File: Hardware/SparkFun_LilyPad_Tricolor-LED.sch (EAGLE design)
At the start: 11 parts

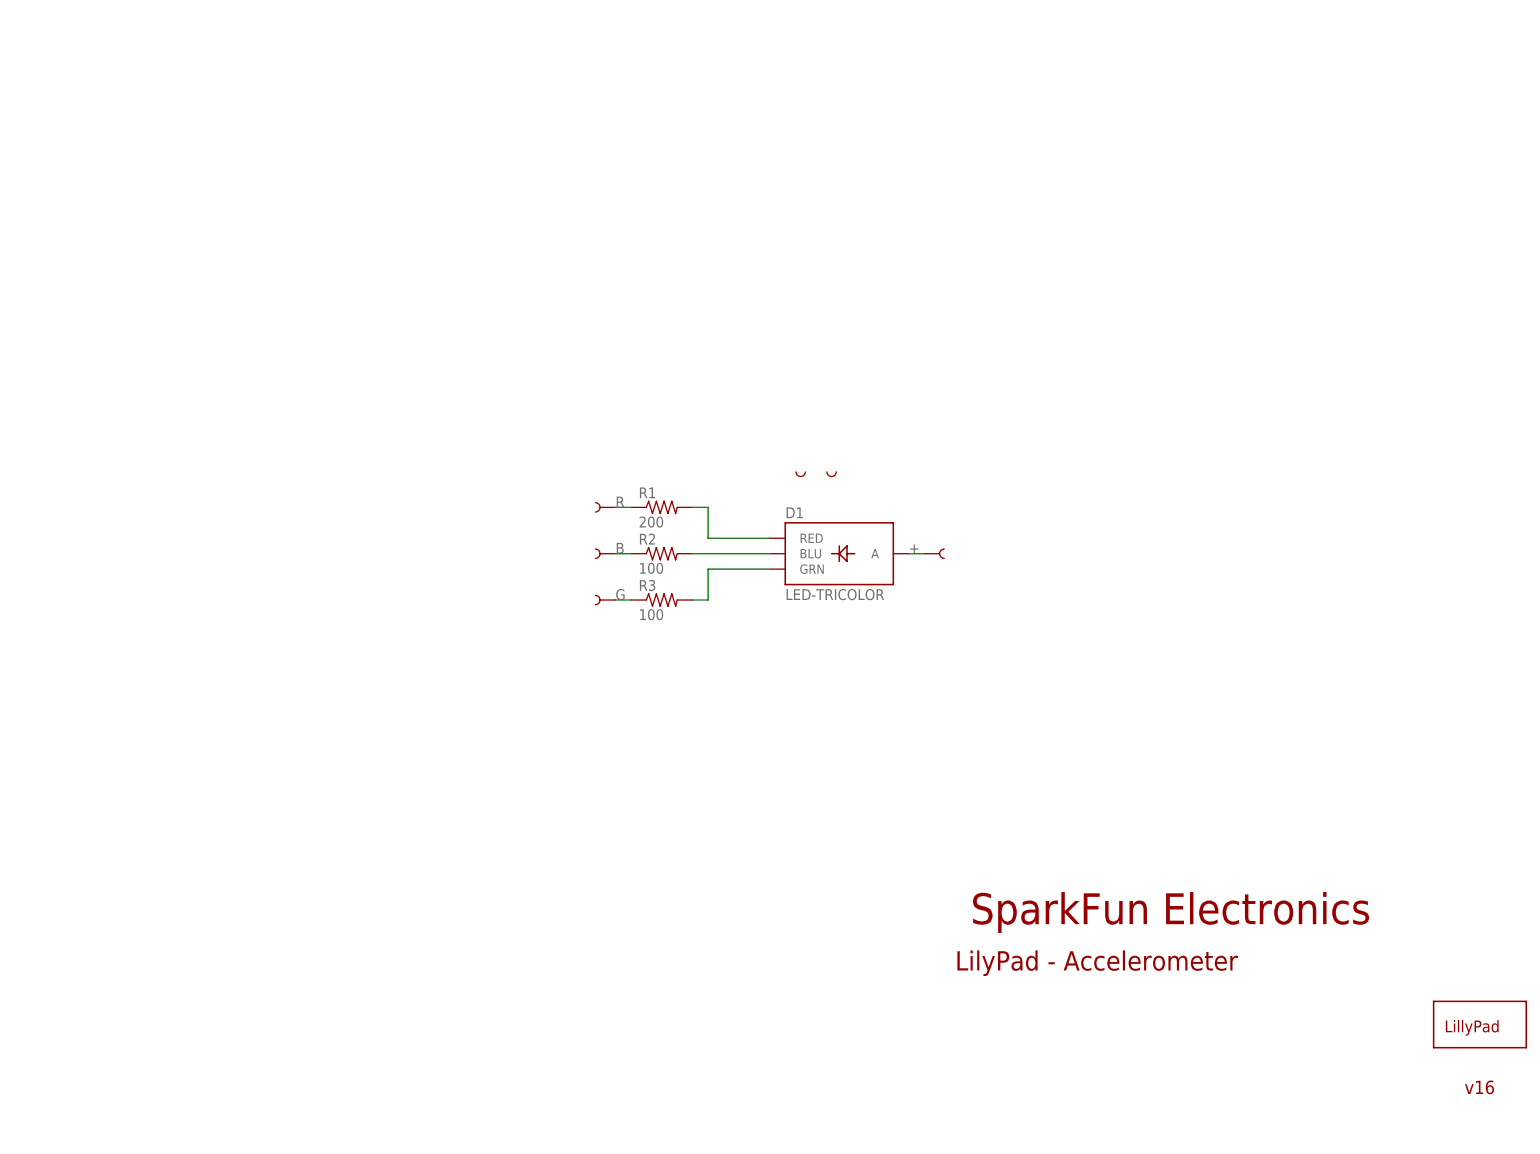
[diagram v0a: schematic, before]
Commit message: revising to common cathode LED
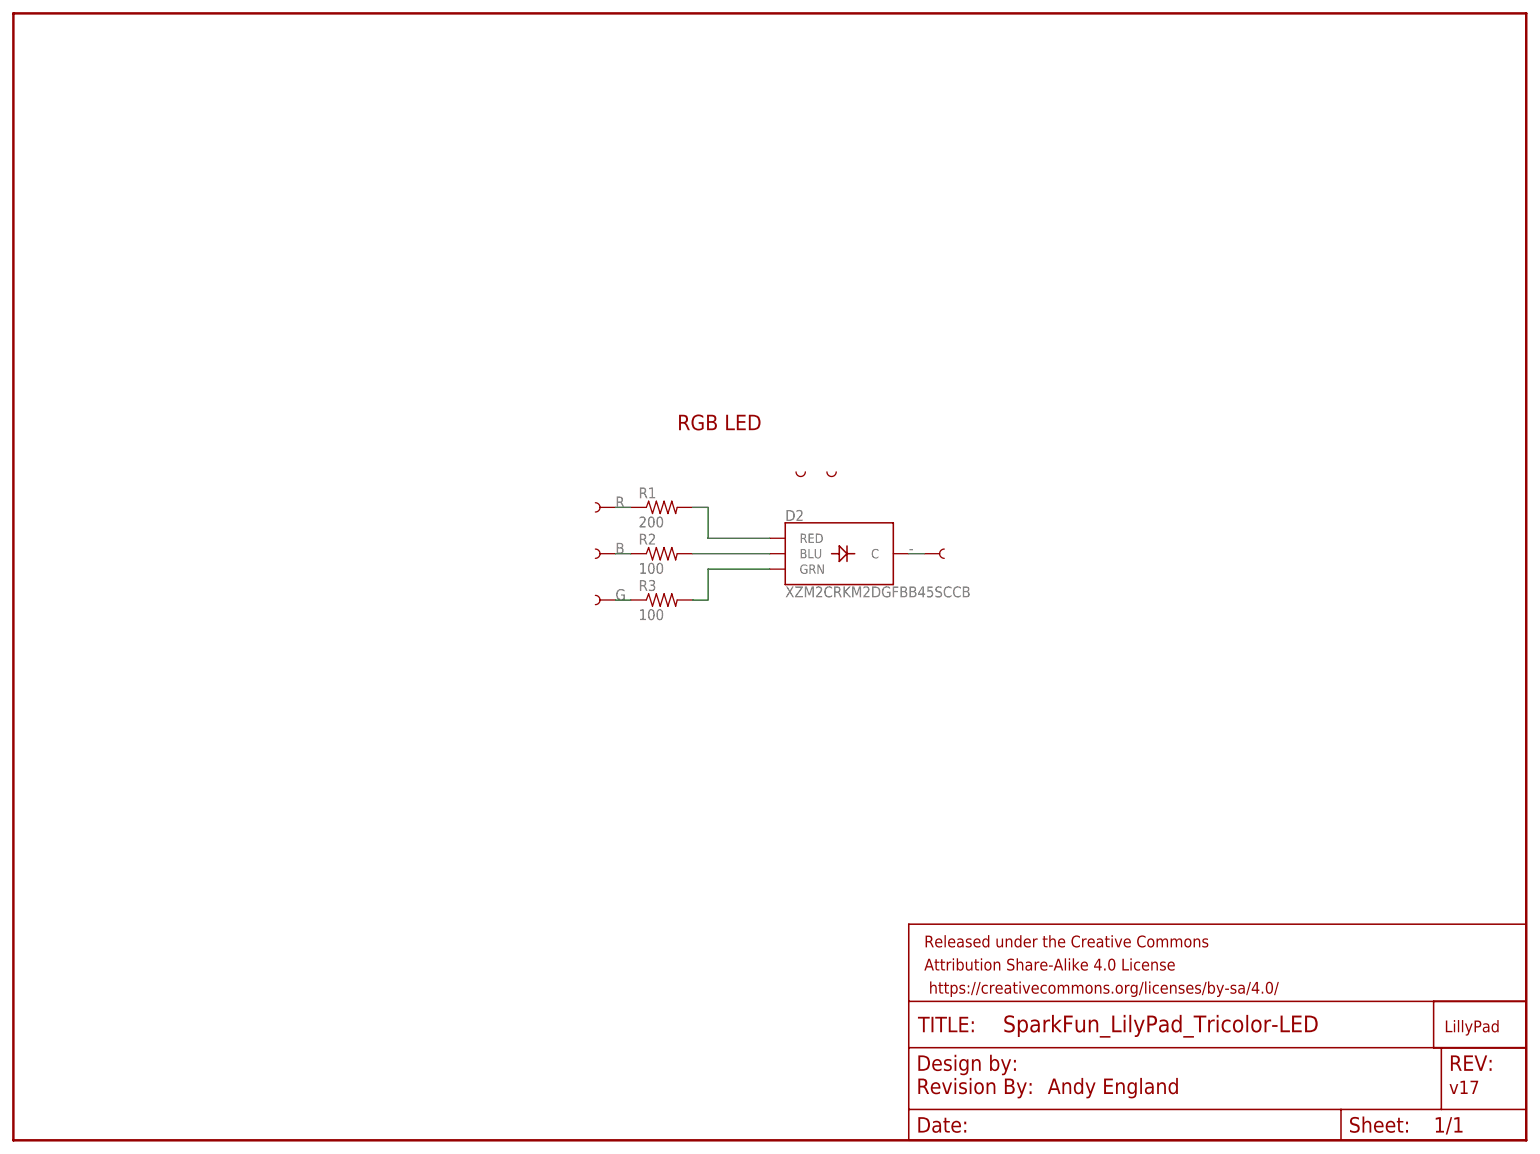
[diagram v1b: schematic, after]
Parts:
- removed D1: LED-TRICOLOR, SparkFun:LED-TRICOLOR
- added D2: XZM2CRKM2DGFBB45SCCB, SparkFun-LED:SUNLEDSMD1
- added FRAME1: FRAME-LETTER, SparkFun-Aesthetics:FRAME-LETTER
- added LOGO1: REVISION, SparkFun-Aesthetics:REVISION
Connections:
- removed net +: D1.A, U$10.1
- new net -: D2.C, U$10.1
- net BLU: now also D2.BLU; no longer D1.BLU
- net GRN: now also D2.GRN; no longer D1.GRN
- net RED: now also D2.RED; no longer D1.RED
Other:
- note added: "Andy England"
- note added: "RGB LED"
- note added: "v17"
- note removed: "LilyPad - Accelerometer"
- note removed: "SparkFun Electronics"
- note removed: "v16"
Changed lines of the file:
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@@
 <?xml version="1.0" encoding="utf-8"?>
 <!DOCTYPE eagle SYSTEM "eagle.dtd">
-<eagle version="7.2.0">
+<eagle version="9.1.0">
 <drawing>
 <settings>
-<setting alwaysvectorfont="yes"/>
+<setting alwaysvectorfont="no"/>
+<setting keepoldvectorfont="yes"/>
 <setting verticaltext="up"/>
 </settings>
@@
 <layer number="54" name="bGND_GNDA" color="1" fill="9" visible="no" active="no"/>
 <layer number="56" name="wert" color="7" fill="1" visible="no" active="no"/>
+<layer number="57" name="tCAD" color="7" fill="1" visible="no" active="no"/>
+<layer number="59" name="tCarbon" color="7" fill="1" visible="no" active="no"/>
+<layer number="60" name="bCarbon" color="7" fill="1" visible="no" active="no"/>
+<layer number="88" name="SimResults" color="9" fill="1" visible="yes" active="yes"/>
+<layer number="89" name="SimProbes" color="9" fill="1" visible="yes" active="yes"/>
+<layer number="90" name="Modules" color="5" fill="1" visible="no" active="no"/>
 <layer number="91" name="Nets" color="2" fill="1" visible="yes" active="yes"/>
 <layer number="92" name="Busses" color="1" fill="1" visible="yes" active="yes"/>
@@
 <layer number="97" name="Info" color="7" fill="1" visible="yes" active="yes"/>
 <layer number="98" name="Guide" color="6" fill="1" visible="yes" active="yes"/>
+<layer number="99" name="SpiceOrder" color="7" fill="1" visible="yes" active="yes"/>
 <layer number="100" name="Muster" color="7" fill="1" visible="no" active="no"/>
 <layer number="101" name="Patch_Top" color="12" fill="4" visible="yes" active="yes"/>
@@
 <layer number="106" name="bPlate" color="7" fill="1" visible="yes" active="yes"/>
 <layer number="107" name="Crop" color="7" fill="1" visible="yes" active="yes"/>
+<layer number="108" name="tplace-old" color="10" fill="1" visible="yes" active="yes"/>
+<layer number="109" name="ref-old" color="11" fill="1" visible="yes" active="yes"/>
+<layer number="110" name="fp0" color="7" fill="1" visible="yes" active="yes"/>
+<layer number="111" name="LPC17xx" color="7" fill="1" visible="yes" active="yes"/>
+<layer number="112" name="tSilk" color="7" fill="1" visible="yes" active="yes"/>
+<layer number="113" name="IDFDebug" color="4" fill="1" visible="yes" active="yes"/>
+<layer number="114" name="Badge_Outline" color="7" fill="1" visible="yes" active="yes"/>
+<layer number="115" name="ReferenceISLANDS" color="7" fill="1" visible="yes" active="yes"/>
 <layer number="116" name="Patch_BOT" color="9" fill="4" visible="yes" active="yes"/>
+<layer number="118" name="Rect_Pads" color="7" fill="1" visible="yes" active="yes"/>
 <layer number="121" name="_tsilk" color="7" fill="1" visible="yes" active="yes"/>
 <layer number="122" name="_bsilk" color="7" fill="1" visible="yes" active="yes"/>
+<layer number="123" name="tTestmark" color="7" fill="1" visible="yes" active="yes"/>
+<layer number="124" name="bTestmark" color="7" fill="1" visible="yes" active="yes"/>
+<layer number="125" name="_tNames" color="7" fill="1" visible="yes" active="yes"/>
+<layer number="126" name="_bNames" color="7" fill="1" visible="yes" active="yes"/>
+<layer number="127" name="_tValues" color="7" fill="1" visible="yes" active="yes"/>
+<layer number="128" name="_bValues" color="7" fill="1" visible="yes" active="yes"/>
+<layer number="129" name="Mask" color="7" fill="1" visible="yes" active="yes"/>
+<layer number="131" name="tAdjust" color="7" fill="1" visible="yes" active="yes"/>
+<layer number="132" name="bAdjust" color="7" fill="1" visible="yes" active="yes"/>
 <layer number="144" name="Drill_legend" color="7" fill="1" visible="yes" active="yes"/>
+<layer number="150" name="Notes" color="7" fill="1" visible="yes" active="yes"/>
 <layer number="151" name="HeatSink" color="7" fill="1" visible="yes" active="yes"/>
+<layer number="152" name="_bDocu" color="7" fill="1" visible="yes" active="yes"/>
+<layer number="153" name="FabDoc1" color="7" fill="1" visible="yes" active="yes"/>
+<layer number="154" name="FabDoc2" color="7" fill="1" visible="yes" active="yes"/>
+<layer number="155" name="FabDoc3" color="7" fill="1" visible="yes" active="yes"/>
+<layer number="199" name="Contour" color="7" fill="1" visible="yes" active="yes"/>
 <layer number="200" name="200bmp" color="1" fill="10" visible="no" active="no"/>
 <layer number="201" name="201bmp" color="2" fill="1" visible="no" active="no"/>
@@
 <layer number="215" name="215bmp" color="7" fill="1" visible="yes" active="yes"/>
 <layer number="216" name="216bmp" color="7" fill="1" visible="yes" active="yes"/>
+<layer number="217" name="217bmp" color="18" fill="1" visible="no" active="no"/>
+<layer number="218" name="218bmp" color="19" fill="1" visible="no" active="no"/>
+<layer number="219" name="219bmp" color="20" fill="1" visible="no" active="no"/>
+<layer number="220" name="220bmp" color="21" fill="1" visible="no" active="no"/>
+<layer number="221" name="221bmp" color="22" fill="1" visible="no" active="no"/>
+<layer number="222" name="222bmp" color="23" fill="1" visible="no" active="no"/>
+<layer number="223" name="223bmp" color="24" fill="1" visible="no" active="no"/>
+<layer number="224" name="224bmp" color="25" fill="1" visible="no" active="no"/>
+<layer number="225" name="225bmp" color="7" fill="1" visible="yes" active="yes"/>
+<layer number="226" name="226bmp" color="7" fill="1" visible="yes" active="yes"/>
+<layer number="227" name="227bmp" color="7" fill="1" visible="yes" active="yes"/>
+<layer number="228" name="228bmp" color="7" fill="1" visible="yes" active="yes"/>
+<layer number="229" name="229bmp" color="7" fill="1" visible="yes" active="yes"/>
+<layer number="230" name="230bmp" color="7" fill="1" visible="yes" active="yes"/>
+<layer number="231" name="231bmp" color="7" fill="1" visible="yes" active="yes"/>
+<layer number="232" name="Eagle3D_PG2" color="7" fill="1" visible="yes" active="yes"/>
+<layer number="233" name="Eagle3D_PG3" color="7" fill="1" visible="yes" active="yes"/>
+<layer number="248" name="Housing" color="7" fill="1" visible="yes" active="yes"/>
+<layer number="249" name="Edge" color="7" fill="1" visible="yes" active="yes"/>
 <layer number="250" name="Descript" color="3" fill="1" visible="no" active="no"/>
 <layer number="251" name="SMDround" color="12" fill="11" visible="no" active="no"/>
 <layer number="254" name="cooling" color="7" fill="1" visible="yes" active="yes"/>
+<layer number="255" name="routoute" color="7" fill="1" visible="yes" active="yes"/>
 </layers>
 <schematic xreflabel="%F%N/%S" xrefpart="/%S.%C%R">
@@
 </classes>
 <parts>
-<part name="D1" library="SparkFun" deviceset="LED-TRICOLOR" device=""/>
 <part name="R1" library="SparkFun" deviceset="RESISTOR" device="0402-RES" value="200"/>
 <part name="R2" library="SparkFun" deviceset="RESISTOR" device="0402-RES" value="100"/>
 <part name="R3" library="SparkFun" deviceset="RESISTOR" device="0402-RES" value="100"/>
-<part name="FRAME1" library="SparkFun" deviceset="FRAME-LETTER" device=""/>
+<part name="FRAME1" library="SparkFun-Aesthetics" deviceset="FRAME-LETTER" device=""/>
 <part name="U$7" library="LilyPad-Wearables" deviceset="SEWTAP" device="6"/>
 <part name="U$8" library="LilyPad-Wearables" deviceset="SEWTAP" device="6"/>
@@
 <part name="U$3" library="LilyPad-Wearables" deviceset="SEWTAP-NOHOLE" device="2"/>
 <part name="U$1" library="LilyPad-Wearables" deviceset="LOGO-LP" device="L"/>
+<part name="D2" library="SparkFun-LED" deviceset="SUNLED" device="SMD1" value="XZM2CRKM2DGFBB45SCCB"/>
+<part name="LOGO1" library="SparkFun-Aesthetics" deviceset="REVISION" device=""/>
 </parts>
 <sheets>
 <sheet>
 <plain>
-<text x="154.94" y="27.94" size="3.175" layer="94">LilyPad - Accelerometer</text>
-<text x="157.48" y="35.56" size="5.08" layer="94">SparkFun Electronics</text>
-<text x="238.76" y="7.62" size="2.1844" layer="94">v16</text>
+<text x="236.22" y="7.62" size="2.1844" layer="94" font="vector">v17</text>
+<text x="170.18" y="7.62" size="2.54" layer="94" font="vector">Andy England</text>
+<text x="109.22" y="116.84" size="2.54" layer="94" font="vector">RGB LED</text>
 </plain>
 <instances>
-<instance part="D1" gate="G$1" x="134.62" y="99.06"/>
 <instance part="R1" gate="G$1" x="106.68" y="104.14"/>
 <instance part="R2" gate="G$1" x="106.68" y="96.52"/>
 <instance part="R3" gate="G$1" x="106.68" y="88.9"/>
 <instance part="FRAME1" gate="G$1" x="0" y="0"/>
-<instance part="FRAME1" gate="G$2" x="147.32" y="0"/>
+<instance part="FRAME1" gate="V" x="147.32" y="0"/>
 <instance part="U$7" gate="G$1" x="96.52" y="104.14" rot="R180"/>
 <instance part="U$8" gate="G$1" x="96.52" y="88.9" rot="R180"/>
@@
 <instance part="U$3" gate="G$1" x="134.62" y="109.22" rot="R90"/>
 <instance part="U$1" gate="G$1" x="236.22" y="17.78"/>
+<instance part="D2" gate="G1" x="134.62" y="96.52"/>
+<instance part="LOGO1" gate="G$1" x="148.59" y="7.62"/>
 </instances>
 <busses>
@@
 <wire x1="114.3" y1="99.06" x2="124.46" y2="99.06" width="0.1524" layer="91"/>
 <pinref part="R1" gate="G$1" pin="2"/>
-<pinref part="D1" gate="G$1" pin="RED"/>
+<pinref part="D2" gate="G1" pin="RED"/>
 </segment>
 </net>
@@
 <wire x1="111.76" y1="96.52" x2="124.46" y2="96.52" width="0.1524" layer="91"/>
 <pinref part="R2" gate="G$1" pin="2"/>
-<pinref part="D1" gate="G$1" pin="BLU"/>
+<pinref part="D2" gate="G1" pin="BLU"/>
 </segment>
 </net>
@@
 <wire x1="114.3" y1="93.98" x2="124.46" y2="93.98" width="0.1524" layer="91"/>
 <pinref part="R3" gate="G$1" pin="2"/>
-<pinref part="D1" gate="G$1" pin="GRN"/>
-</segment>
-</net>
-<net name="+" class="0">
+<pinref part="D2" gate="G1" pin="GRN"/>
+</segment>
+</net>
+<net name="-" class="0">
 <segment>
 <wire x1="149.86" y1="96.52" x2="147.32" y2="96.52" width="0.1524" layer="91"/>
 <label x="147.32" y="96.52" size="1.778" layer="95"/>
-<pinref part="D1" gate="G$1" pin="A"/>
 <pinref part="U$10" gate="G$1" pin="1"/>
-</segment>
-</net>
+<pinref part="D2" gate="G1" pin="C"/>
+</segment>
+</net>
